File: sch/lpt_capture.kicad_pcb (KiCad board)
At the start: 2 copper layers, 2 parts, among them J1 DB25_Male_MountingHoles

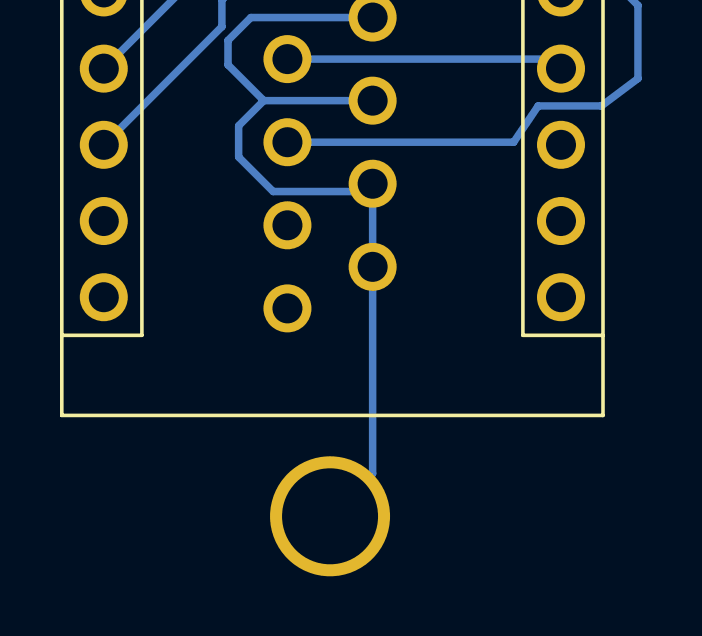
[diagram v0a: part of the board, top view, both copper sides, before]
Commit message: Add 1K resistors and a note to schematic.
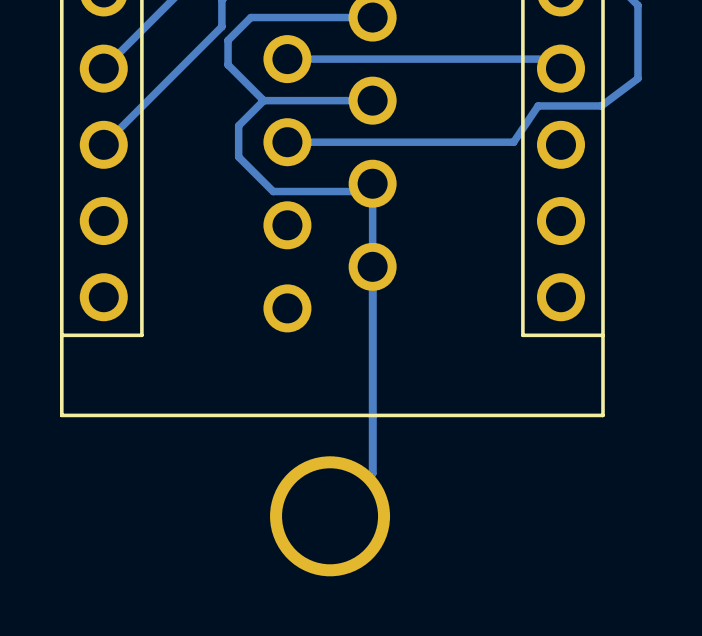
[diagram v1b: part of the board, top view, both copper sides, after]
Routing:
- net GND: track 82.6 -> 89.5 mm

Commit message: Do the PCB.
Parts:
- added R1: 1K, Resistor_THT:R_Axial_DIN0207_L6.3mm_D2.5mm_P7.62mm_Horizontal, F.Cu at (114.3, 91.4)
- added R2: 1K, Resistor_THT:R_Axial_DIN0207_L6.3mm_D2.5mm_P7.62mm_Horizontal, F.Cu at (114.3, 94.0)
- added R3: 1K, Resistor_THT:R_Axial_DIN0207_L6.3mm_D2.5mm_P7.62mm_Horizontal, F.Cu at (114.3, 96.5)
- added R4: 1K, Resistor_THT:R_Axial_DIN0207_L6.3mm_D2.5mm_P7.62mm_Horizontal, F.Cu at (114.3, 100.3)
- added R5: 1K, Resistor_THT:R_Axial_DIN0207_L6.3mm_D2.5mm_P7.62mm_Horizontal, F.Cu at (114.3, 104.1)
- added R6: 1K, Resistor_THT:R_Axial_DIN0207_L6.3mm_D2.5mm_P7.62mm_Horizontal, F.Cu at (114.3, 108.0)
- added R7: 1K, Resistor_THT:R_Axial_DIN0207_L6.3mm_D2.5mm_P7.62mm_Horizontal, F.Cu at (114.3, 111.8)
- added R8: 1K, Resistor_THT:R_Axial_DIN0207_L6.3mm_D2.5mm_P7.62mm_Horizontal, F.Cu at (114.3, 115.6)
- added R9: 1K, Resistor_THT:R_Axial_DIN0207_L6.3mm_D2.5mm_P7.62mm_Horizontal, F.Cu at (115.6, 119.4)
- added U2: 74LS541, Package_DIP:DIP-20_W7.62mm_LongPads, F.Cu at (179.1, 118.4)
- J1: footprint Connector_Dsub:DSUB-25_Male_Vertical_P2.77x2.84mm_MountingHoles -> Connector_Dsub:DSUB-25_Male_Horizontal_P2.77x2.84mm_EdgePinOffset4.94mm_Housed_MountingHolesOffset7.48mm; moved to F.Cu
- moved A1 42.2 mm to (102.4, 121.9), turned to 180 degrees
- moved J1 32.9 mm to (119.4, 119.4), turned to 90 degrees
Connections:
- net Net-(A1-Pad19) renamed /PC0
- net Net-(A1-Pad20) renamed /PC1
- A1 pad 10: Net-(A1-Pad10) -> /PD7
- A1 pad 11: Net-(A1-Pad11) -> /PB0
- A1 pad 12: Net-(A1-Pad12) -> /PB1
- A1 pad 13: Net-(A1-Pad13) -> /PB2
- A1 pad 5: Net-(A1-Pad5) -> /PD2(INT0)
- A1 pad 6: Net-(A1-Pad6) -> /PD3
- A1 pad 7: Net-(A1-Pad7) -> /PD4
- A1 pad 8: Net-(A1-Pad8) -> /PD5
- A1 pad 9: Net-(A1-Pad9) -> /PD6
- J1 pad 1: Net-(A1-Pad5) -> Net-(J1-Pad1)
- J1 pad 12: (no net) -> GND
- J1 pad 2: Net-(A1-Pad6) -> Net-(J1-Pad2)
- J1 pad 3: Net-(A1-Pad7) -> Net-(J1-Pad3)
- J1 pad 4: Net-(A1-Pad8) -> Net-(J1-Pad4)
- J1 pad 5: Net-(A1-Pad9) -> Net-(J1-Pad5)
- J1 pad 6: Net-(A1-Pad10) -> Net-(J1-Pad6)
- J1 pad 7: Net-(A1-Pad11) -> Net-(J1-Pad7)
- J1 pad 8: Net-(A1-Pad12) -> Net-(J1-Pad8)
- J1 pad 9: Net-(A1-Pad13) -> Net-(J1-Pad9)
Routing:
- net GND: track 89.5 -> 20.4 mm
- net /PC1: track 17.8 -> 52.3 mm
- net /PC0: track 9.25 -> 35.6 mm
- net Net-(A1-Pad5): track 10.0 -> 0.00 mm
- net /PD2(INT0): track 0.00 -> 9.93 mm
- net Net-(A1-Pad6): track 9.77 -> 0.00 mm
- net Net-(A1-Pad7): track 9.54 -> 0.00 mm
- net Net-(A1-Pad8): track 9.31 -> 0.00 mm
- net Net-(A1-Pad9): track 9.08 -> 0.00 mm
- net Net-(A1-Pad12): track 9.04 -> 0.00 mm
- net Net-(A1-Pad13): track 8.97 -> 0.00 mm
- net Net-(A1-Pad10): track 8.85 -> 0.00 mm
- net Net-(A1-Pad11): track 8.64 -> 0.00 mm
- net Net-(J1-Pad7): track 0.00 -> 8.34 mm
- net /PD3: track 0.00 -> 8.14 mm
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- added copper zone on B.Cu, net GND
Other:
- board outline added: 43.2 x 55.9 mm
- board text added: "LPT CAPTURE V1 (C)2022 mikee@saxicola.co.uk"
